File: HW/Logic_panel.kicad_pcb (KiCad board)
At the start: 2 copper layers, 90 x 99 mm, 239 parts, among them J1 USB_B_Micro, Q1 Q_NPN_BCE, Q2 Q_NPN_BCE, Q3 Q_PMOS_DGS, Q4 Q_PMOS_DGS, Q7 Q_PMOS_DGS, SW1 SW_SPDT, SW10 button, SW11 button, SW12 button, SW2 button, SW3 button, SW4 button, SW5 button, SW6 button, SW7 button, SW8 button, SW9 button, U1 ESP32-PICO-D4, U2 CP2102N-A01-GQFN28, U3 SY8105, U4 Dual_battery, U5 TP4056

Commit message: ready for first prototype
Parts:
- removed the REF** at (113.5, 134.8)
- removed the REF** at (119.0, 134.8)
- removed the REF** at (119.7, 134.8)
- removed the REF** at (120.3, 134.8)
- removed the REF** at (120.9, 134.8)
- removed the REF** at (121.5, 134.8)
- removed the REF** at (91.0, 134.8)
- removed the REF** at (91.6, 134.8)
- removed the REF** at (92.2, 134.8)
- removed the REF** at (92.8, 134.8)
- removed the REF** at (93.5, 134.8)
- removed the REF** at (114.1, 134.8)
- removed the REF** at (94.1, 134.8)
- removed the REF** at (94.7, 134.8)
- removed the REF** at (95.3, 134.8)
- removed the REF** at (95.9, 134.8)
- removed the REF** at (96.5, 134.8)
- removed the REF** at (97.2, 134.8)
- removed the REF** at (97.8, 134.8)
- removed the REF** at (98.4, 134.8)
- removed the REF** at (99.0, 134.8)
- removed the REF** at (68.5, 134.8)
- removed the REF** at (114.7, 134.8)
- removed the REF** at (69.1, 134.8)
- removed the REF** at (69.7, 134.8)
- removed the REF** at (70.3, 134.8)
- removed the REF** at (71.0, 134.8)
- removed the REF** at (71.6, 134.8)
- removed the REF** at (72.2, 134.8)
- removed the REF** at (72.8, 134.8)
- removed the REF** at (73.4, 134.8)
- removed the REF** at (74.0, 134.8)
- removed the REF** at (74.7, 134.8)
- removed the REF** at (115.3, 134.8)
- removed the REF** at (75.3, 134.8)
- removed the REF** at (75.9, 134.8)
- removed the REF** at (76.5, 134.8)
- removed the REF** at (121.5, 50.2)
- removed the REF** at (120.9, 50.2)
- removed the REF** at (120.3, 50.2)
- removed the REF** at (119.7, 50.2)
- removed the REF** at (119.0, 50.2)
- removed the REF** at (118.4, 50.2)
- removed the REF** at (117.8, 50.2)
- removed the REF** at (116.0, 134.8)
- removed the REF** at (117.2, 50.2)
- removed the REF** at (116.6, 50.2)
- removed the REF** at (116.0, 50.2)
- removed the REF** at (115.3, 50.2)
- removed the REF** at (114.7, 50.2)
- removed the REF** at (114.1, 50.2)
- removed the REF** at (113.5, 50.2)
- removed the REF** at (99.0, 50.2)
- removed the REF** at (98.4, 50.2)
- removed the REF** at (97.8, 50.2)
- removed the REF** at (116.6, 134.8)
- removed the REF** at (97.2, 50.2)
- removed the REF** at (96.5, 50.2)
- removed the REF** at (95.9, 50.2)
- removed the REF** at (95.3, 50.2)
- removed the REF** at (94.7, 50.2)
- removed the REF** at (94.1, 50.2)
- removed the REF** at (93.5, 50.2)
- removed the REF** at (92.8, 50.2)
- removed the REF** at (92.2, 50.2)
- removed the REF** at (91.6, 50.2)
- removed the REF** at (117.2, 134.8)
- removed the REF** at (91.0, 50.2)
- removed the REF** at (76.5, 50.2)
- removed the REF** at (75.9, 50.2)
- removed the REF** at (75.3, 50.2)
- removed the REF** at (74.7, 50.2)
- removed the REF** at (74.0, 50.2)
- removed the REF** at (73.4, 50.2)
- removed the REF** at (72.8, 50.2)
- removed the REF** at (72.2, 50.2)
- removed the REF** at (71.6, 50.2)
- removed the REF** at (117.8, 134.8)
- removed the REF** at (71.0, 50.2)
- removed the REF** at (70.3, 50.2)
- removed the REF** at (69.7, 50.2)
- removed the REF** at (69.1, 50.2)
- removed the REF** at (68.5, 50.2)
- removed the REF** at (55.0, 139.5)
- removed the REF** at (135.0, 45.5)
- removed the REF** at (55.0, 45.5)
- removed the REF** at (118.4, 134.8)
- added REF**: NPTH, NPTH, F.Cu at (115.4, 132.2)
- added REF**: NPTH, NPTH, F.Cu at (120.9, 132.2)
- added REF**: NPTH, NPTH, F.Cu at (121.5, 132.2)
- added REF**: NPTH, NPTH, F.Cu at (122.2, 132.2)
- added REF**: NPTH, NPTH, F.Cu at (122.8, 132.2)
- added REF**: NPTH, NPTH, F.Cu at (123.4, 132.2)
- added REF**: NPTH, NPTH, F.Cu at (92.3, 132.2)
- added REF**: NPTH, NPTH, F.Cu at (92.9, 132.2)
- added REF**: NPTH, NPTH, F.Cu at (93.5, 132.2)
- added REF**: NPTH, NPTH, F.Cu at (94.1, 132.2)
- added REF**: NPTH, NPTH, F.Cu at (94.7, 132.2)
- added REF**: NPTH, NPTH, F.Cu at (116.0, 132.2)
- added REF**: NPTH, NPTH, F.Cu at (95.3, 132.2)
- added REF**: NPTH, NPTH, F.Cu at (96.0, 132.2)
- added REF**: NPTH, NPTH, F.Cu at (96.6, 132.2)
- added REF**: NPTH, NPTH, F.Cu at (97.2, 132.2)
- added REF**: NPTH, NPTH, F.Cu at (97.8, 132.2)
- added REF**: NPTH, NPTH, F.Cu at (98.4, 132.2)
- added REF**: NPTH, NPTH, F.Cu at (99.0, 132.2)
- added REF**: NPTH, NPTH, F.Cu at (99.6, 132.2)
- added REF**: NPTH, NPTH, F.Cu at (100.3, 132.2)
- added REF**: NPTH, NPTH, F.Cu at (69.1, 132.2)
- added REF**: NPTH, NPTH, F.Cu at (116.6, 132.2)
- added REF**: NPTH, NPTH, F.Cu at (69.7, 132.2)
- added REF**: NPTH, NPTH, F.Cu at (70.4, 132.2)
- added REF**: NPTH, NPTH, F.Cu at (71.0, 132.2)
- added REF**: NPTH, NPTH, F.Cu at (71.6, 132.2)
- added REF**: NPTH, NPTH, F.Cu at (72.2, 132.2)
- added REF**: NPTH, NPTH, F.Cu at (72.8, 132.2)
- added REF**: NPTH, NPTH, F.Cu at (73.4, 132.2)
- added REF**: NPTH, NPTH, F.Cu at (74.1, 132.2)
- added REF**: NPTH, NPTH, F.Cu at (74.7, 132.2)
- added REF**: NPTH, NPTH, F.Cu at (75.3, 132.2)
- added REF**: NPTH, NPTH, F.Cu at (117.2, 132.2)
- added REF**: NPTH, NPTH, F.Cu at (75.9, 132.2)
- added REF**: NPTH, NPTH, F.Cu at (76.5, 132.2)
- added REF**: NPTH, NPTH, F.Cu at (77.1, 132.2)
- added REF**: NPTH, NPTH, F.Cu at (123.4, 50.3)
- added REF**: NPTH, NPTH, F.Cu at (122.8, 50.3)
- added REF**: NPTH, NPTH, F.Cu at (122.2, 50.3)
- added REF**: NPTH, NPTH, F.Cu at (121.6, 50.3)
- added REF**: NPTH, NPTH, F.Cu at (120.9, 50.3)
- added REF**: NPTH, NPTH, F.Cu at (120.3, 50.3)
- added REF**: NPTH, NPTH, F.Cu at (119.7, 50.3)
- added REF**: NPTH, NPTH, F.Cu at (117.9, 132.2)
- added REF**: NPTH, NPTH, F.Cu at (119.1, 50.3)
- added REF**: NPTH, NPTH, F.Cu at (118.5, 50.3)
- added REF**: NPTH, NPTH, F.Cu at (117.9, 50.3)
- added REF**: NPTH, NPTH, F.Cu at (117.2, 50.3)
- added REF**: NPTH, NPTH, F.Cu at (116.6, 50.3)
- added REF**: NPTH, NPTH, F.Cu at (116.0, 50.3)
- added REF**: NPTH, NPTH, F.Cu at (115.4, 50.3)
- added REF**: NPTH, NPTH, F.Cu at (100.3, 50.3)
- added REF**: NPTH, NPTH, F.Cu at (99.6, 50.3)
- added REF**: NPTH, NPTH, F.Cu at (99.0, 50.3)
- added REF**: NPTH, NPTH, F.Cu at (118.5, 132.2)
- added REF**: NPTH, NPTH, F.Cu at (98.4, 50.3)
- added REF**: NPTH, NPTH, F.Cu at (97.8, 50.3)
- added REF**: NPTH, NPTH, F.Cu at (97.2, 50.3)
- added REF**: NPTH, NPTH, F.Cu at (96.6, 50.3)
- added REF**: NPTH, NPTH, F.Cu at (96.0, 50.3)
- added REF**: NPTH, NPTH, F.Cu at (95.3, 50.3)
- added REF**: NPTH, NPTH, F.Cu at (94.7, 50.3)
- added REF**: NPTH, NPTH, F.Cu at (94.1, 50.3)
- added REF**: NPTH, NPTH, F.Cu at (93.5, 50.3)
- added REF**: NPTH, NPTH, F.Cu at (92.9, 50.3)
- added REF**: NPTH, NPTH, F.Cu at (119.1, 132.2)
- added REF**: NPTH, NPTH, F.Cu at (92.3, 50.3)
- added REF**: NPTH, NPTH, F.Cu at (77.1, 50.3)
- added REF**: NPTH, NPTH, F.Cu at (76.5, 50.3)
- added REF**: NPTH, NPTH, F.Cu at (75.9, 50.3)
- added REF**: NPTH, NPTH, F.Cu at (75.3, 50.3)
- added REF**: NPTH, NPTH, F.Cu at (74.7, 50.3)
- added REF**: NPTH, NPTH, F.Cu at (74.1, 50.3)
- added REF**: NPTH, NPTH, F.Cu at (73.4, 50.3)
- added REF**: NPTH, NPTH, F.Cu at (72.8, 50.3)
- added REF**: NPTH, NPTH, F.Cu at (72.2, 50.3)
- added REF**: NPTH, NPTH, F.Cu at (119.7, 132.2)
- added REF**: NPTH, NPTH, F.Cu at (71.6, 50.3)
- added REF**: NPTH, NPTH, F.Cu at (71.0, 50.3)
- added REF**: NPTH, NPTH, F.Cu at (70.4, 50.3)
- added REF**: NPTH, NPTH, F.Cu at (69.7, 50.3)
- added REF**: NPTH, NPTH, F.Cu at (69.1, 50.3)
- added REF**: NPTH, NPTH, F.Cu at (55.0, 137.0)
- added REF**: NPTH, NPTH, F.Cu at (137.5, 45.5)
- added REF**: NPTH, NPTH, F.Cu at (55.0, 45.5)
- added REF**: NPTH, NPTH, F.Cu at (120.3, 132.2)
- C18: footprint Capacitor_SMD:C_1206_3216Metric -> Capacitor_SMD:C_0402_1005Metric
- moved C18 1.98 mm to (74.0, 65.2)
- moved C115 1.10 mm to (136.2, 89.8)
- moved D123 1.10 mm to (136.0, 111.2)
- moved Q7 1.10 mm to (130.9, 68.8)
- moved R18 1.10 mm to (129.9, 72.0)
- moved C10 1.10 mm to (96.4, 78.9)
- moved C109 1.10 mm to (113.6, 89.8)
- moved C11 1.10 mm to (121.5, 129.3)
- moved C113 1.10 mm to (128.7, 89.8)
- moved C127 1.10 mm to (120.9, 106.5)
- moved C17 1.10 mm to (71.6, 129.4)
- moved C19 1.10 mm to (74.0, 64.1)
- moved C29 1.10 mm to (71.1, 90.2)
- moved C31 1.10 mm to (79.3, 90.2)
- moved C32 1.10 mm to (88.6, 129.4)
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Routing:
- net Board_1-+3V3: track 69.8 -> 105.9 mm, vias 4 -> 8
- net Board_1-GND: track 1027.7 -> 1063.0 mm, vias 10 -> 35
- net Board_1-V_BAT_1: track 402.9 -> 423.3 mm, vias 2 -> 6
- net Board_1-V_BAT_SPINANE: track 101.2 -> 108.8 mm, vias 0 -> 2
- net Board_1-BTN_END: track 67.4 -> 62.9 mm
- net Board_1-BTN_NEW_GAME: track 70.6 -> 66.1 mm
- net Board_1-DATA_zadani_LED: track 51.9 -> 48.0 mm
- net Board_1-BARVA_5: track 105.9 -> 103.9 mm
- net Board_1-VBUS: track 121.7 -> 119.7 mm, vias 8 -> 9
- net Board_1-ZAPINANI_2_CAST_LED: track 45.4 -> 43.9 mm
- net Board_1-ZAPINANI_1_CAST_LED: track 53.3 -> 52.1 mm
- net Board_1-BARVA_1: track 139.5 -> 139.0 mm
- net Board_1-RX_ESP: track 46.7 -> 47.2 mm
- added copper zone on B.Cu, net Board_1-GND
- added copper zone on F.Cu, net Board_1-GND
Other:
- board size 90 x 99 mm -> 92.5 x 96.5 mm

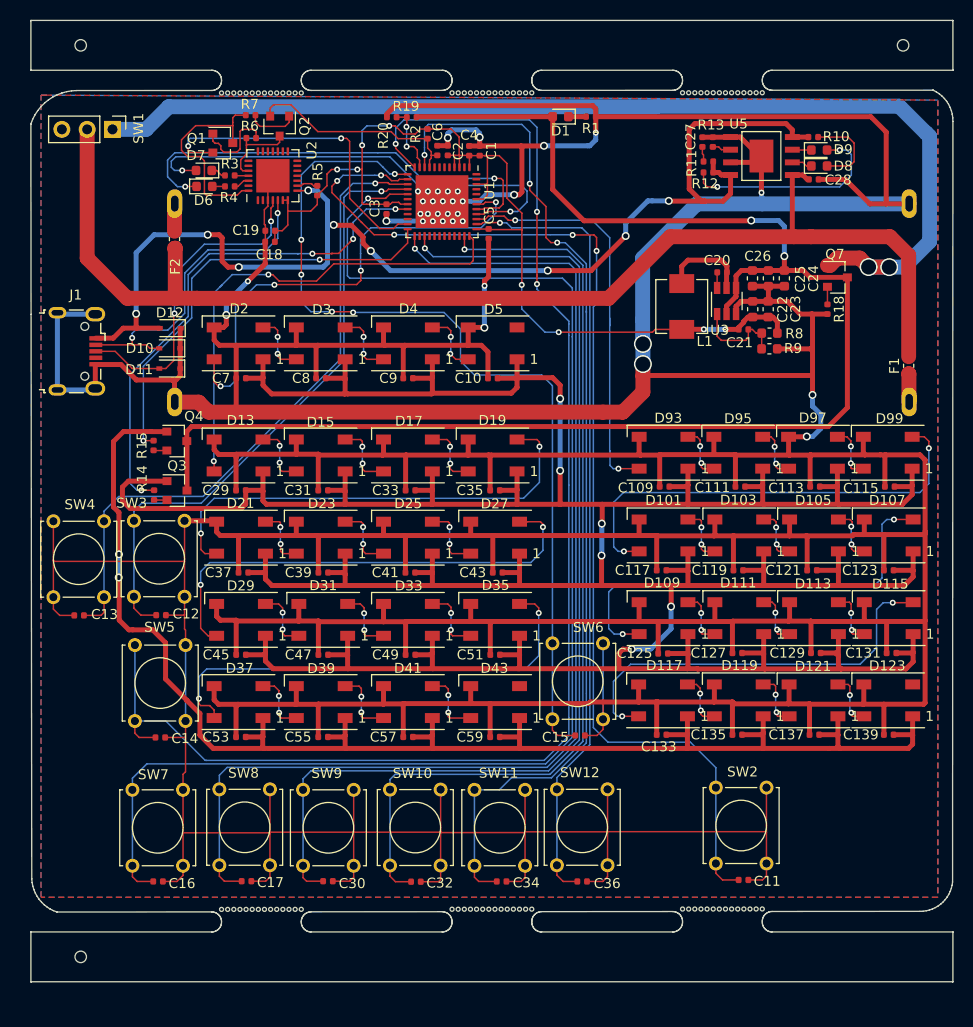
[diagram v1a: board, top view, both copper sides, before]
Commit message: add mounting holes, repair gitignore
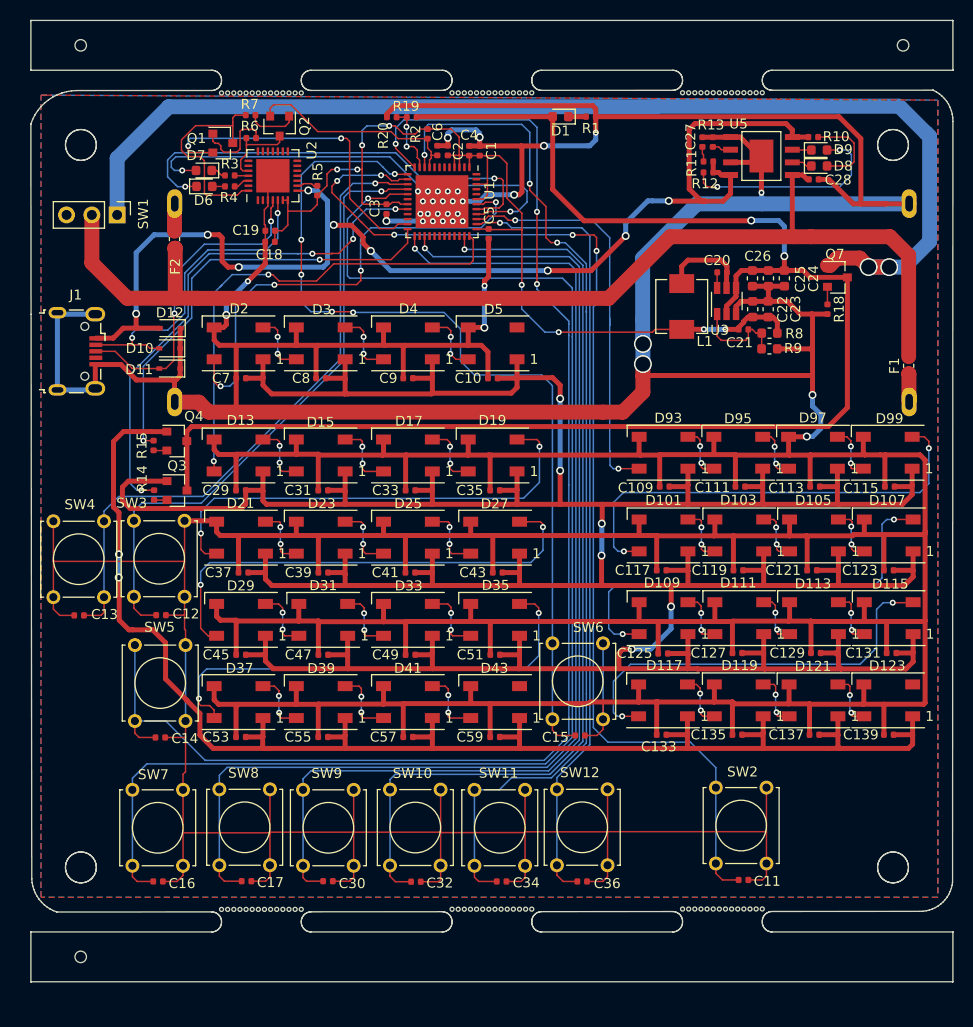
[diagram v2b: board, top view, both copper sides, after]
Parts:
- moved SW1 8.60 mm to (58.7, 62.5)
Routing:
- net Board_1-V_BAT_PRIME: track 123.7 -> 115.0 mm
- net Board_1-V_BAT_SPINANE: track 108.8 -> 115.3 mm
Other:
- outline, holes or cut-outs redrawn
